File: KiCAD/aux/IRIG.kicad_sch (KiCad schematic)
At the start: 10 parts, among them J7 Conn_Coaxial_Small, T5 LM-NP-1001-B1L, U6 OPA171AIDBVR, U7 DAC121S101CIMKX_NOPB

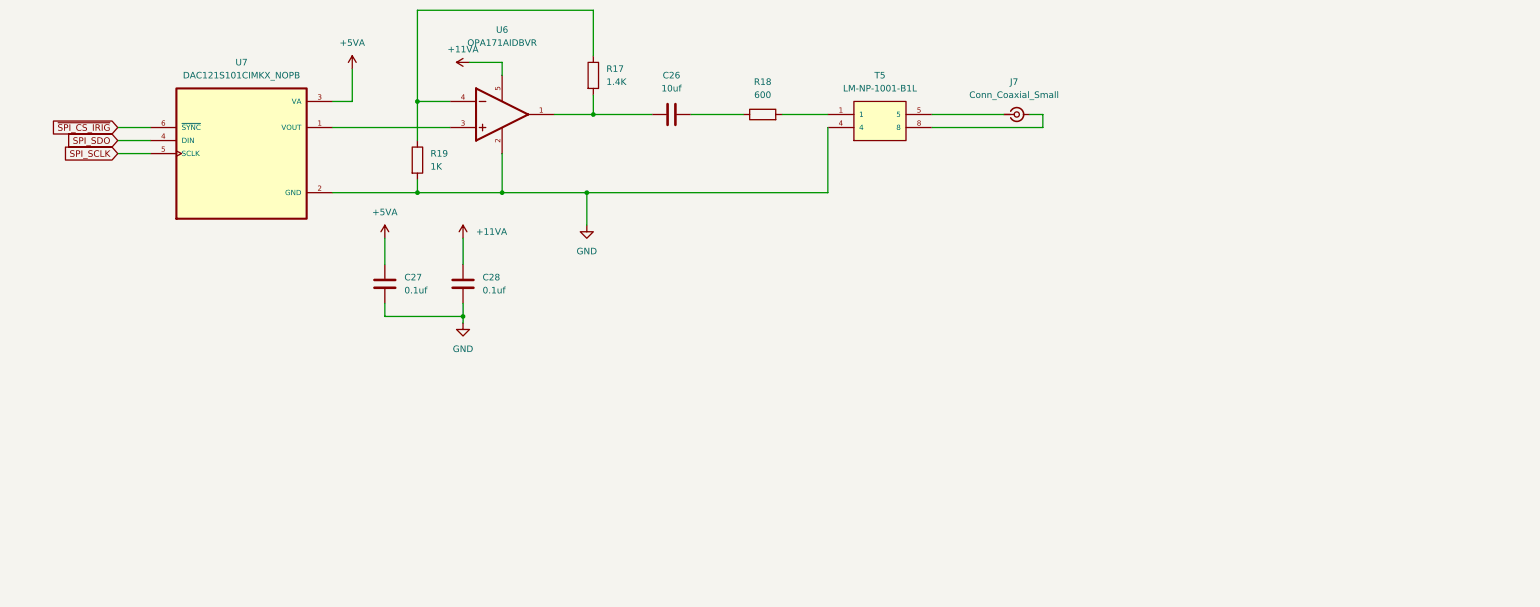
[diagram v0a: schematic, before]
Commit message: Reworked, now with IRIG option board complete
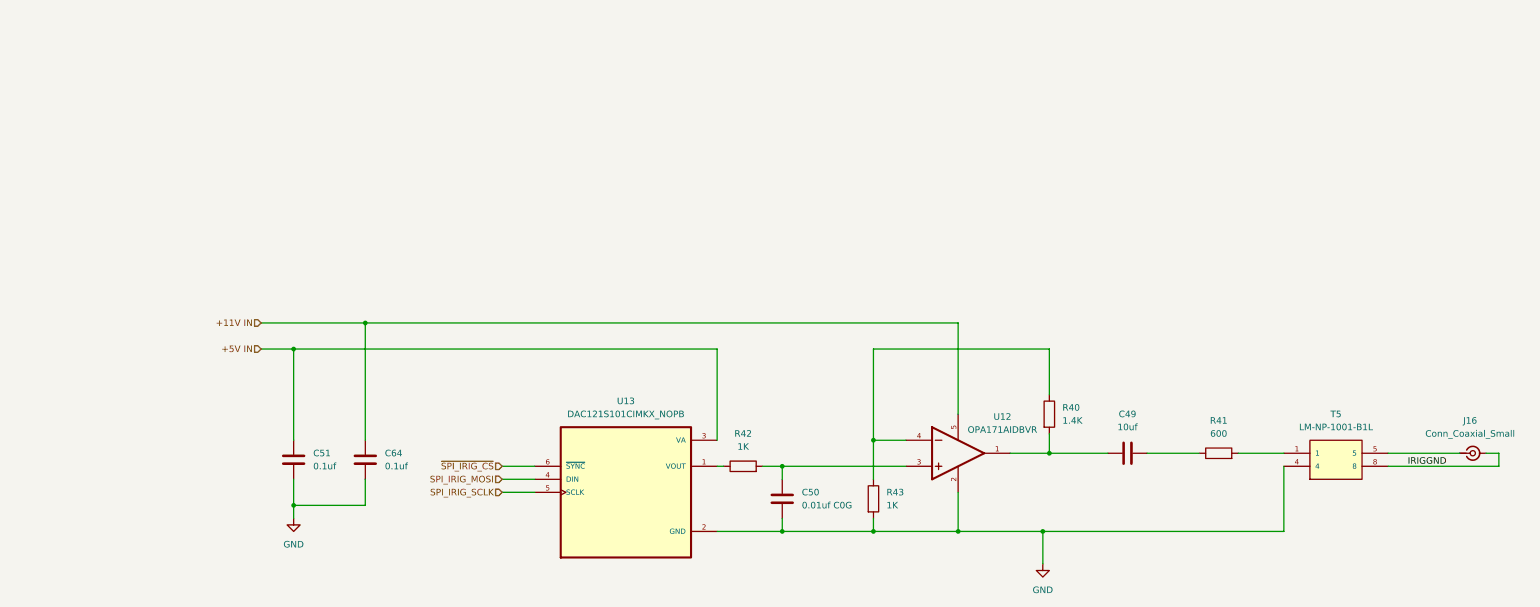
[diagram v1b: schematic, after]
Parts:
- removed C28: 0.1uf, Capacitor_SMD:C_1206_3216Metric_Pad1.33x1.80mm_HandSolder, symbol Device:C
- added C50: 0.01uf C0G, Capacitor_SMD:C_1206_3216Metric_Pad1.33x1.80mm_HandSolder, symbol Device:C
- added C64: 0.1uf, Capacitor_SMD:C_1206_3216Metric_Pad1.33x1.80mm_HandSolder, symbol Device:C
- added R42: 1K, Resistor_SMD:R_1206_3216Metric_Pad1.30x1.75mm_HandSolder, symbol Device:R
- renumbered C26 to C49, C27 to C51, J7 to J16, R17 to R40, R18 to R41, R19 to R43, U6 to U12, U7 to U13
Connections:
- net GND: now also C50.2, C64.2
- net at U12.3: now also C50.1, R42.2; no longer U13.1 (VOUT)
- net IRIGGND: now reaches J16.2 (Ext), T5.8
- net +11VA renamed +11V IN
- net +11V IN: now also C64.1
- net +5VA renamed +5V IN
- net SPI_SCLK renamed SPI_IRIG_SCLK
- net SPI_SDO renamed SPI_IRIG_MOSI
- net ~{SPI_CS_IRIG} renamed ~{SPI_IRIG_CS}
- new net: R42.1, U13.1 (VOUT)
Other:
- moved on the sheet: C49, C51, J16, R40, R41, R43, T5, U12, U13
